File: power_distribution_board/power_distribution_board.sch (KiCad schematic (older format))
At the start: 22 parts

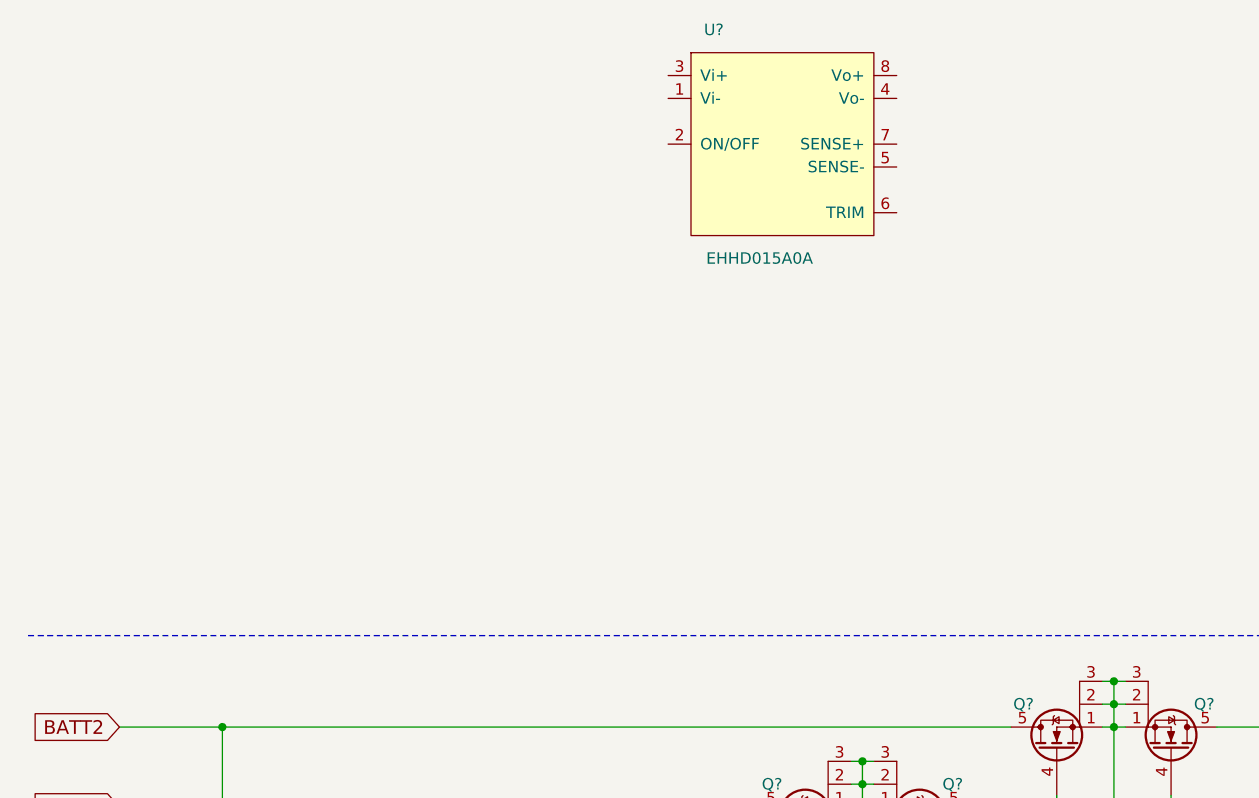
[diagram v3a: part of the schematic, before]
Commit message: add 5v converter module
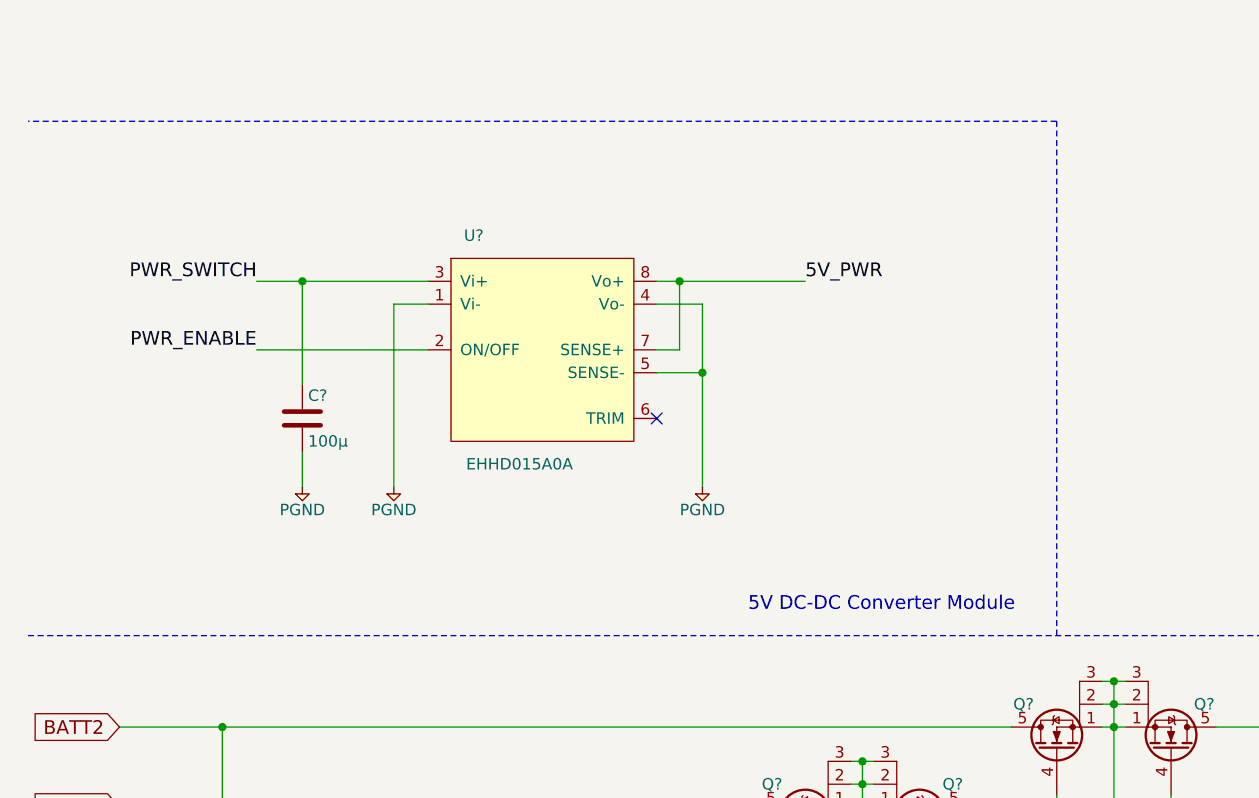
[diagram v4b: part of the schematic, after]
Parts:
- added C?: 100μ, symbol C
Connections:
- net PWR_ENABLE: now also U?.2 (ON/OFF)
- net PGND: now reaches U?.1 (Vi-)
- net PGND: now also U?.4 (Vo-), U?.5 (SENSE-), C?.2
- net PWR_SWITCH: now reaches U?.3 (Vi+)
- net PWR_SWITCH: now also C?.1
- net 5V_PWR: now reaches U?.7 (SENSE+)
- net 5V_PWR: now also U?.8 (Vo+)
- no-connect marks 0 -> 1
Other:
- note added: "5V DC-DC Converter Module"
- moved on the sheet: U?
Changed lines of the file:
@@
 LIBS:cauv_lib
 LIBS:agg-kicad
+LIBS:power_distribution_board-cache
 EELAYER 25 0
 EELAYER END
@@
 L EHHD015A0A U?
 U 1 1 597F4834
-P 3800 2650
-F 0 "U?" H 3500 3150 50  0000 C CNN
-F 1 "EHHD015A0A" H 3700 2150 50  0000 C CNN
-F 2 "" H 3500 2600 50  0001 C CNN
-F 3 "" H 3500 2600 50  0001 C CNN
-	1    3800 2650
+P 2750 3550
+F 0 "U?" H 2450 4050 50  0000 C CNN
+F 1 "EHHD015A0A" H 2650 3050 50  0000 C CNN
+F 2 "" H 2450 3500 50  0001 C CNN
+F 3 "" H 2450 3500 50  0001 C CNN
+	1    2750 3550
 	1    0    0    -1
 $EndComp
@@
 Wire Notes Line
 	7700 4800 7700 6500
+$Comp
+L PGND #PWR?
+U 1 1 597F94B7
+P 2100 4150
+F 0 "#PWR?" H 1970 4190 50  0001 L CNN
+F 1 "PGND" H 2100 4050 50  0000 C CNN
+F 2 "" H 2100 4150 60  0001 C CNN
+F 3 "" H 2100 4150 60  0001 C CNN
+	1    2100 4150
+	1    0    0    -1
+$EndComp
+Wire Wire Line
+	1500 3250 2250 3250
+Wire Wire Line
+	2250 3350 2100 3350
+Wire Wire Line
+	2100 3350 2100 4150
+Text Label 1500 3250 2    60   ~ 0
+PWR_SWITCH
+$Comp
+L PGND #PWR?
+U 1 1 59808FC9
+P 3450 4150
+F 0 "#PWR?" H 3320 4190 50  0001 L CNN
+F 1 "PGND" H 3450 4050 50  0000 C CNN
+F 2 "" H 3450 4150 60  0001 C CNN
+F 3 "" H 3450 4150 60  0001 C CNN
+	1    3450 4150
+	1    0    0    -1
+$EndComp
+Wire Wire Line
+	3250 3350 3450 3350
+Wire Wire Line
+	3450 3350 3450 4150
+Wire Wire Line
+	3250 3650 3450 3650
+Connection ~ 3450 3650
+Wire Wire Line
+	3250 3250 3900 3250
+Wire Wire Line
+	3250 3550 3350 3550
+Wire Wire Line
+	3350 3550 3350 3250
+Connection ~ 3350 3250
+NoConn ~ 3250 3850
+$Comp
+L C C?
+U 1 1 5980971D
+P 1700 3850
+F 0 "C?" H 1725 3950 50  0000 L CNN
+F 1 "100μ" H 1725 3750 50  0000 L CNN
+F 2 "" H 1738 3700 50  0001 C CNN
+F 3 "" H 1700 3850 50  0001 C CNN
+	1    1700 3850
+	1    0    0    -1
+$EndComp
+$Comp
+L PGND #PWR?
+U 1 1 5980976A
+P 1700 4150
+F 0 "#PWR?" H 1570 4190 50  0001 L CNN
+F 1 "PGND" H 1700 4050 50  0000 C CNN
+F 2 "" H 1700 4150 60  0001 C CNN
+F 3 "" H 1700 4150 60  0001 C CNN
+	1    1700 4150
+	1    0    0    -1
+$EndComp
+Wire Wire Line
+	1700 4150 1700 4000
+Wire Wire Line
+	1700 3700 1700 3250
+Connection ~ 1700 3250
+Wire Wire Line
+	1500 3550 2250 3550
+Text Label 1500 3550 2    60   ~ 0
+PWR_ENABLE
+Text Label 3900 3250 0    60   ~ 0
+5V_PWR
+Wire Notes Line
+	5000 4800 5000 2550
+Wire Notes Line
+	5000 2550 500  2550
+Text Notes 3650 4700 0    60   ~ 0
+5V DC-DC Converter Module
 $EndSCHEMATC

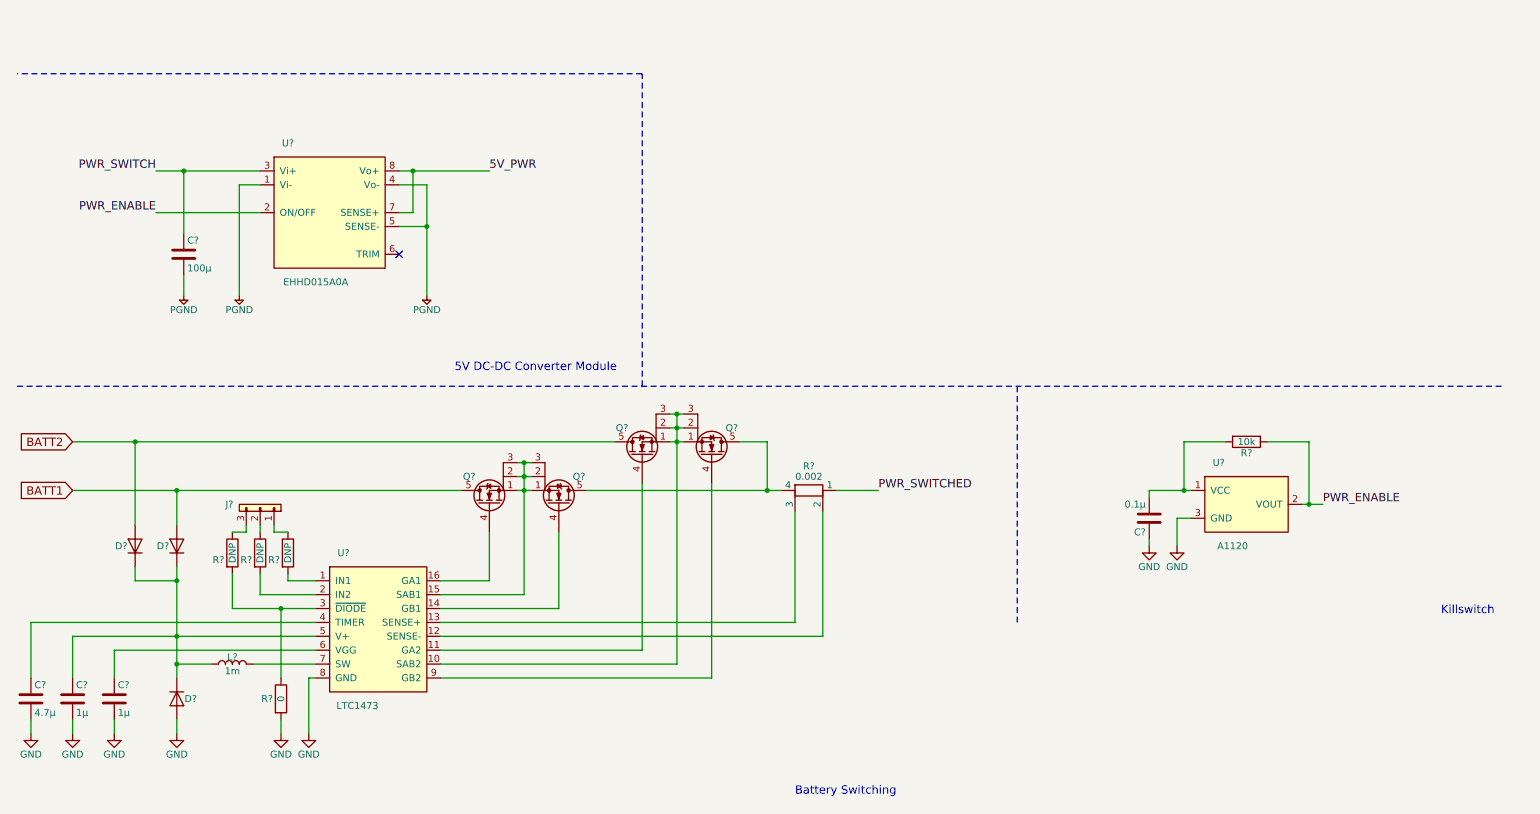
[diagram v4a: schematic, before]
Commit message: add 12v converter module
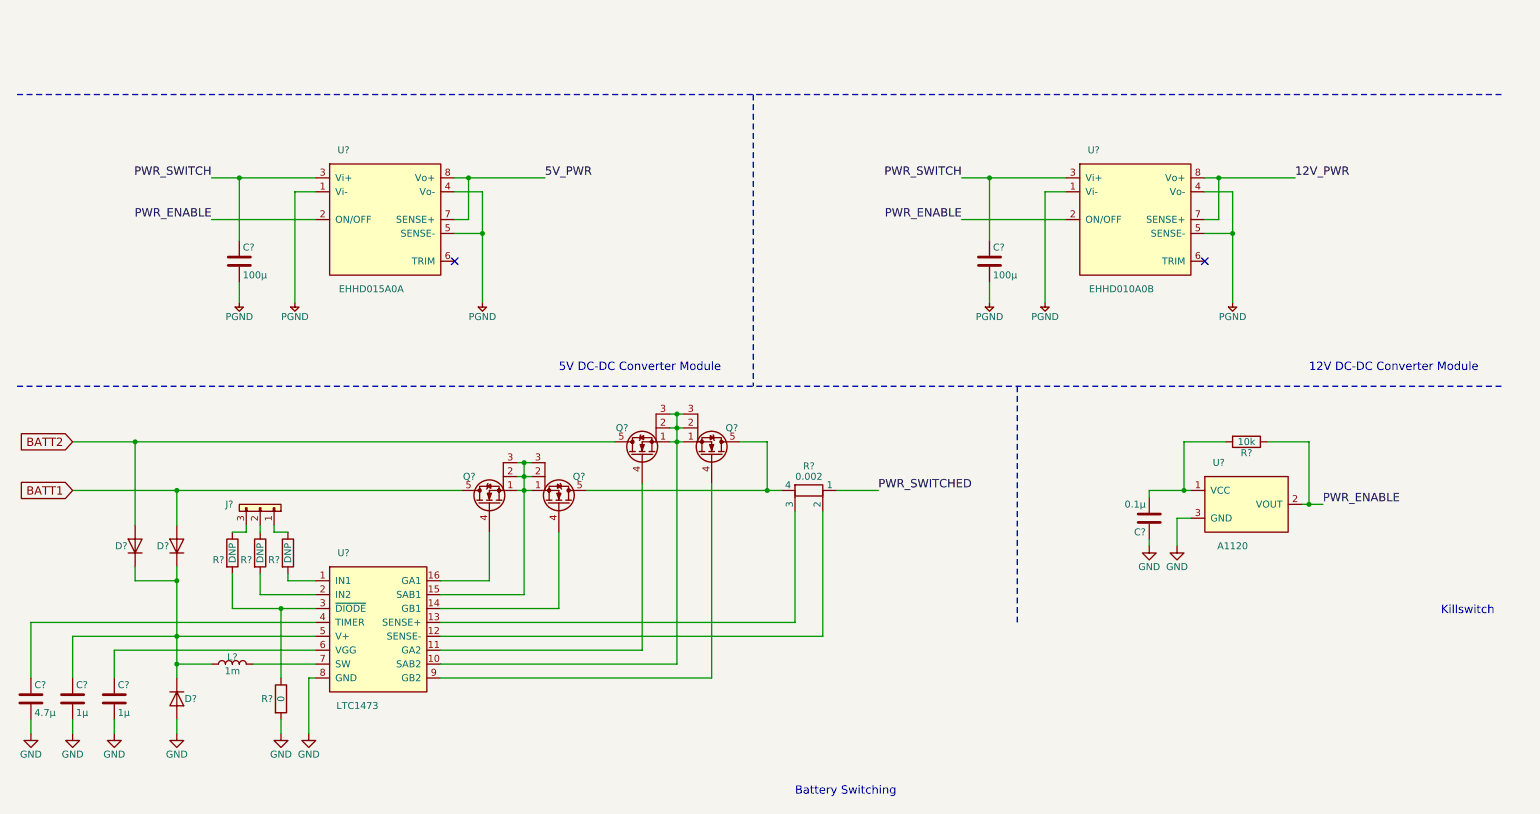
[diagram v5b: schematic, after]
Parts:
- added C?: 100μ, symbol C
- added U?: EHHD010A0B, symbol EHHD010A0B
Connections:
- net PGND: now also C?.2, U?.1 (Vi-), U?.4 (Vo-), U?.5 (SENSE-)
- net PWR_ENABLE: now also U?.2 (ON/OFF)
- net PWR_SWITCH: now also C?.1, U?.3 (Vi+)
- new net 12V_PWR: U?.7 (SENSE+), U?.8 (Vo+)
- no-connect marks 1 -> 2
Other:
- note added: "12V DC-DC Converter Module"
- moved on the sheet: C?, U?

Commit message: add power supply (via lm317) to killswitch
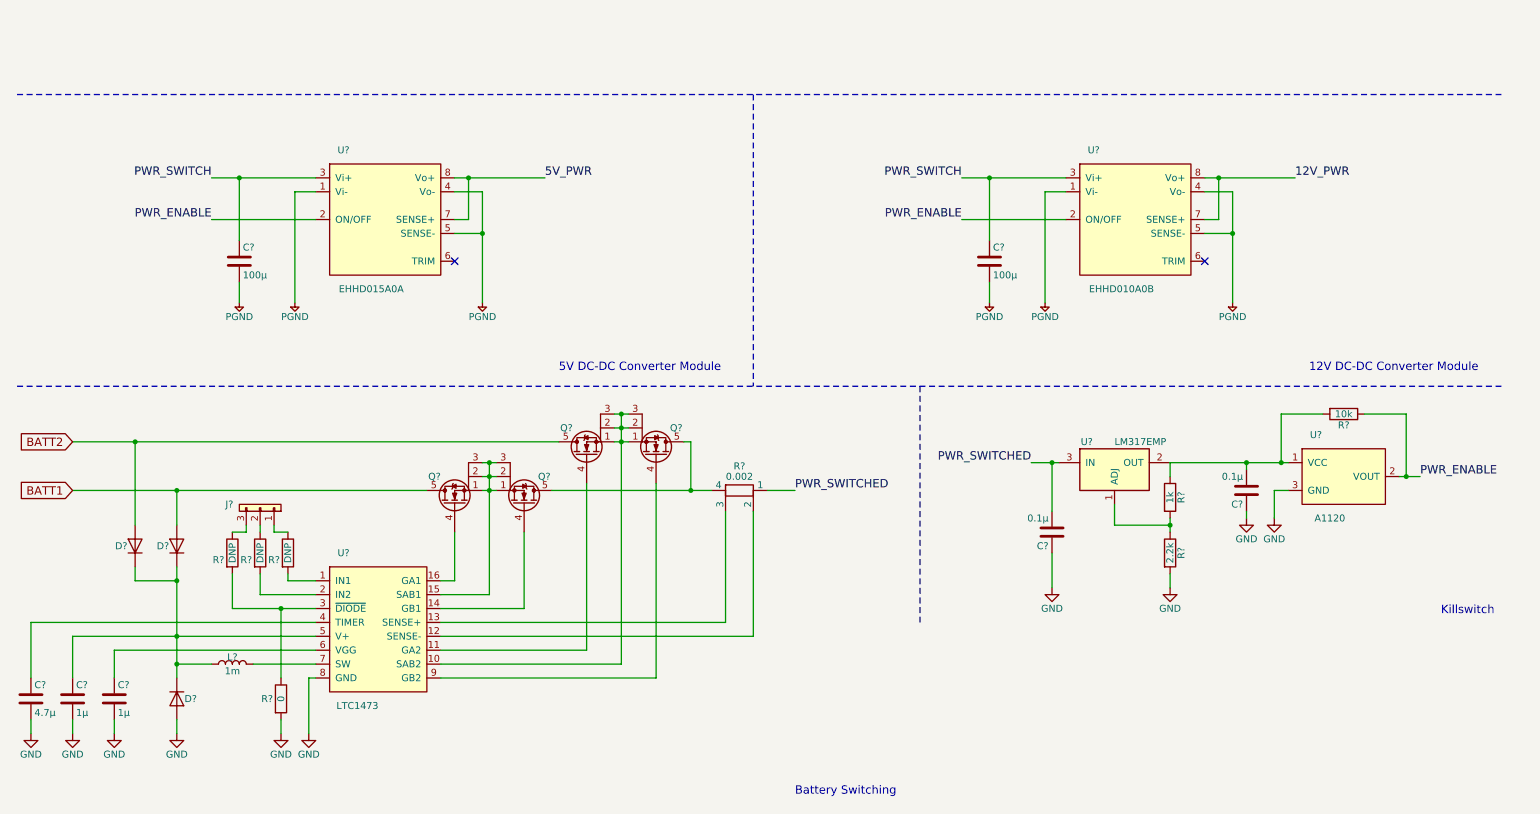
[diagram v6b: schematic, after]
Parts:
- added C?: 0.1μ, symbol C
- added R?: 1k, symbol R
- added R?: 2.2k, symbol R
- added U?: LM317EMP, TO_SOT_Packages_SMD:SOT-223, symbol LM317EMP
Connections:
- net GND: now also C?.1, R?.2
- net PWR_SWITCHED: now also C?.2, U?.3 (IN)
- net at C?.2, R?.2, U?.1 (VCC): now also R?.1, U?.2 (OUT)
- new net: R?.1, R?.2, U?.1 (ADJ)
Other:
- moved on the sheet: C?, Q?, R?, U?
